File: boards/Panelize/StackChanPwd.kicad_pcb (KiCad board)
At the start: 2 copper layers, 50 x 87 mm, 45 parts, among them CN1 B2PS-VH, CN1 PinHeader, CN2 Grove, CN2 PinSocket, CN3 B3B-ZR, CN3 PinHeader, CN4 B3B-ZR, CN4 PinHeader, CN5 B3B-ZR, CN5 PinHeader, CN6 B3B-ZR, CN6 Grove, CN7 Grove, CN8 Grove, U1 74LVC2G125, U1 OKL-T/3-W12N, U2 74HCT2G125, U3 PCA9685PW

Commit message: fix panelized PCB
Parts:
- CN6: footprint Connector_JST:JST_PH_B4B-PH-K_1x04_P2.00mm_Vertical -> Grove:GROVE-HW4-2.0
- moved CN6 3.00 mm to (94.5, 88.0), turned to -90 degrees
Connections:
- CN6 pad 1: GND -> /SERIAL1
- CN6 pad 2: +5VM -> /SERIAL2
- CN6 pad 3: /SERIAL2 -> +5VM
- CN6 pad 4: /SERIAL1 -> GND
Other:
- rule pad_to_mask_clearance: 0 -> 0.051

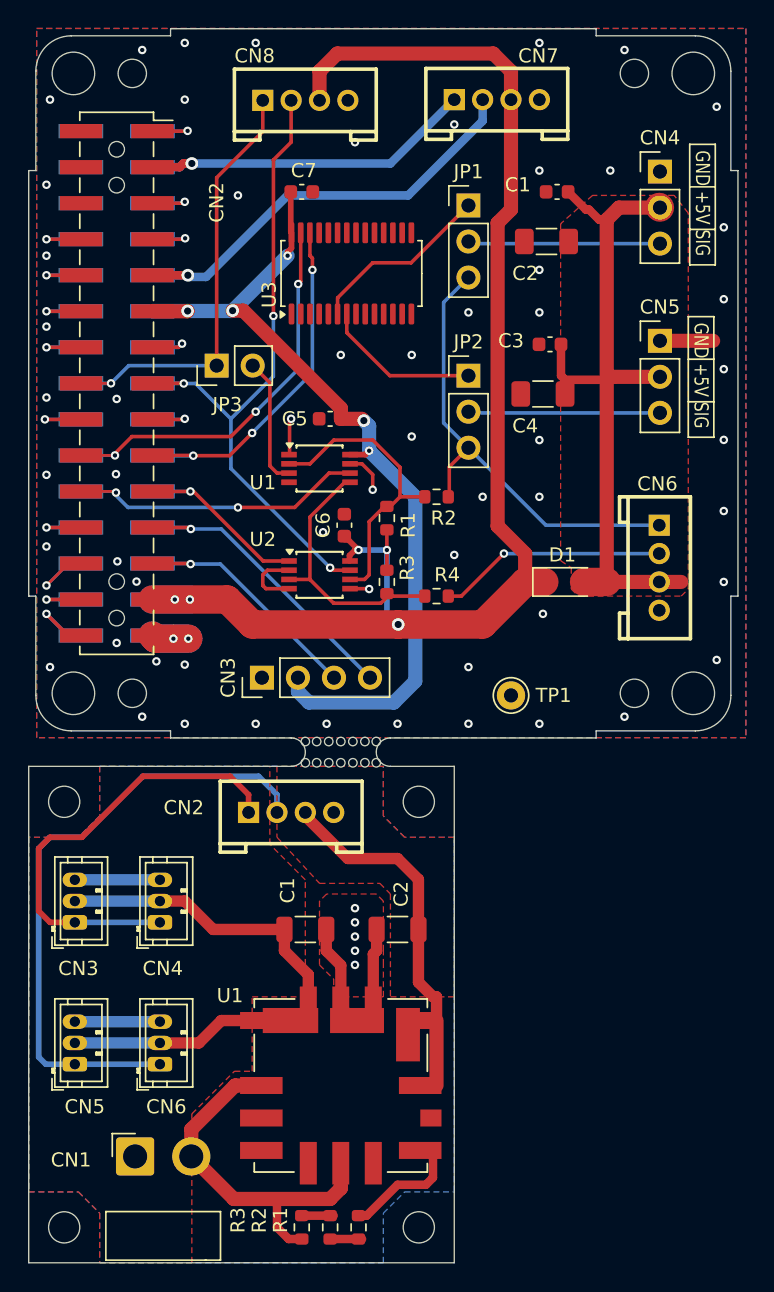
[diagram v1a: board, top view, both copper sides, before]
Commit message: fix PCB design (product ver1.0)
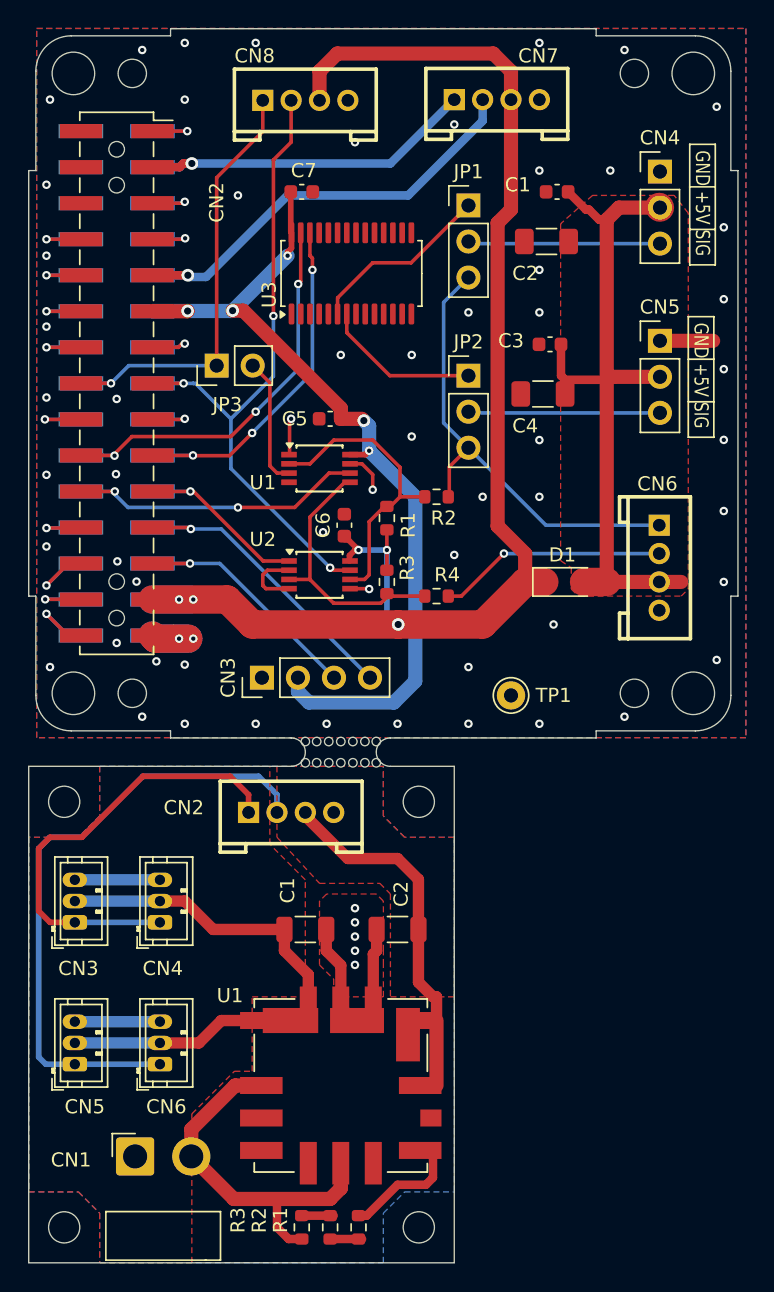
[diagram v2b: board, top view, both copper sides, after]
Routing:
- net /RXD2: track 32.9 -> 32.2 mm

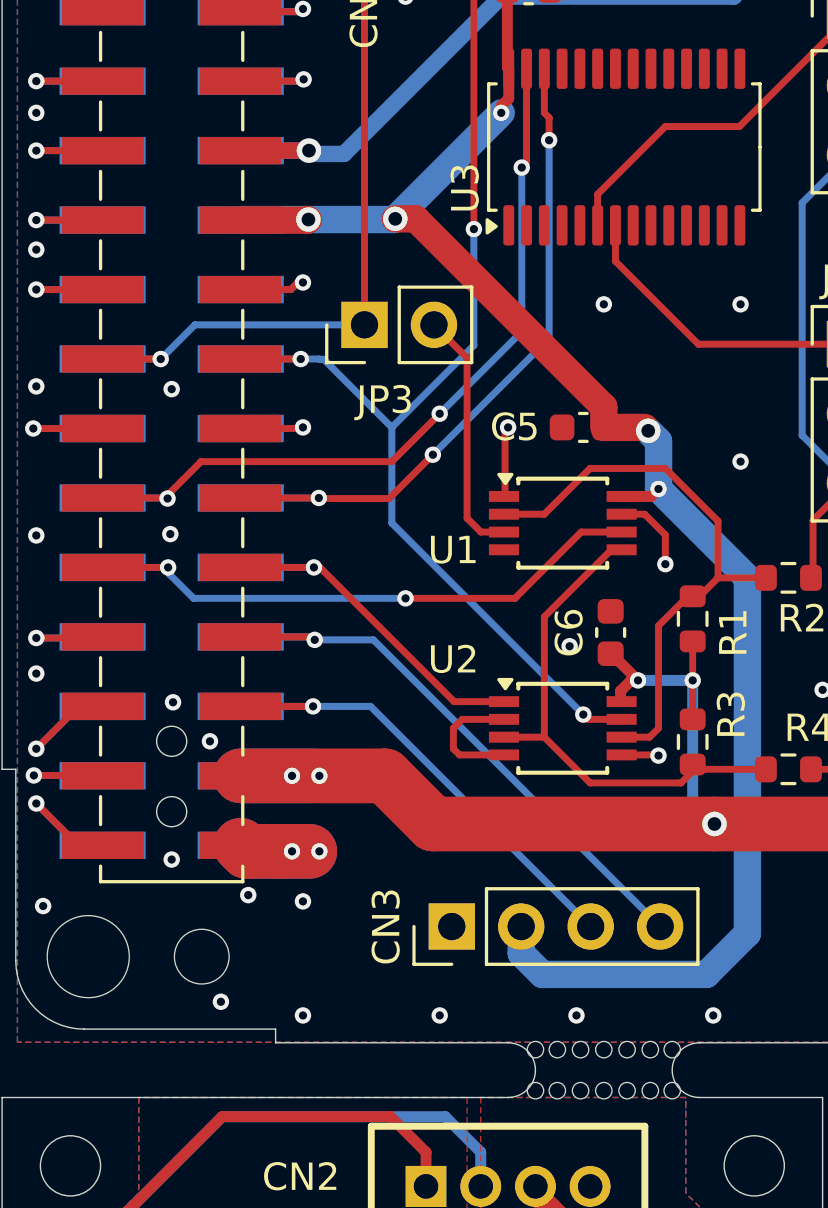
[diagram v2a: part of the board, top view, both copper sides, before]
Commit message: fix panelized PCB design
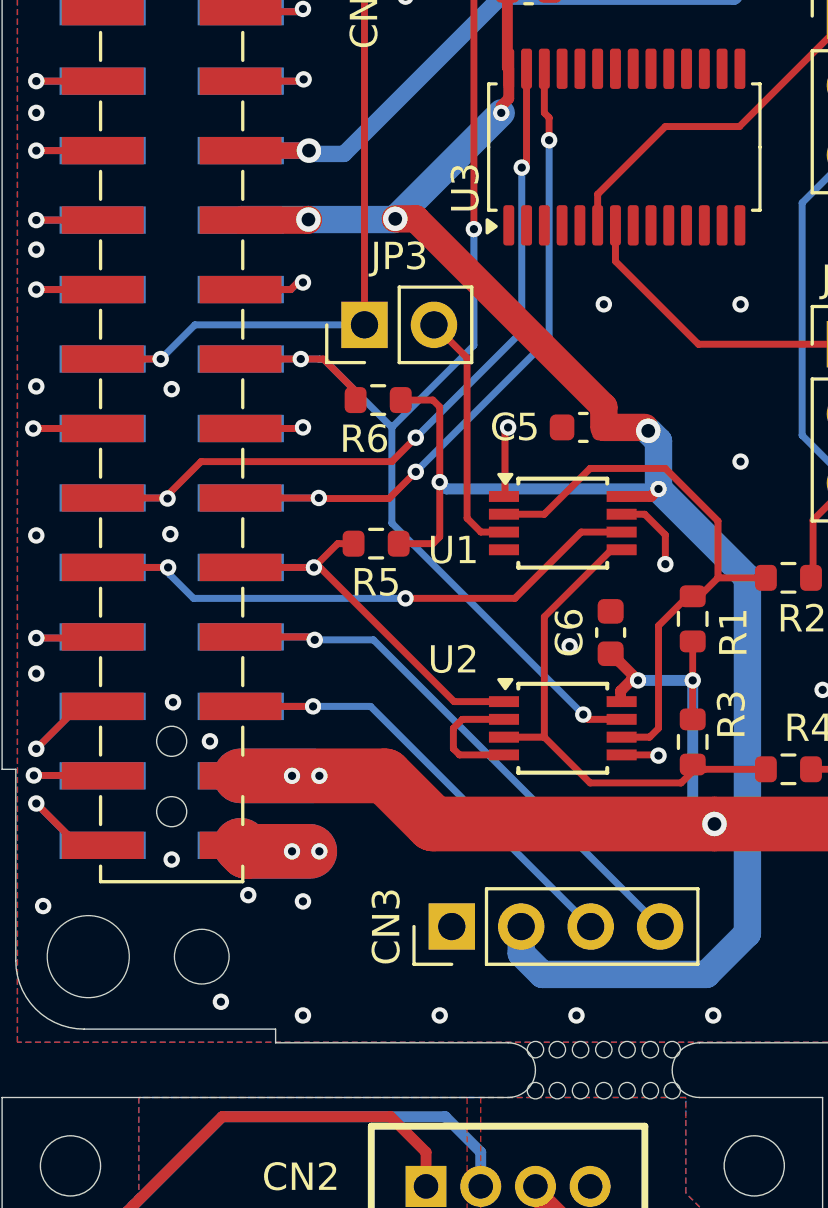
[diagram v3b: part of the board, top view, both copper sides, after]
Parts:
- added R5: 1k, Resistor_SMD:R_0603_1608Metric, F.Cu at (63.7, 81.8)
- added R6: 1k, Resistor_SMD:R_0603_1608Metric, F.Cu at (63.8, 76.5)
- CN4, CN5: value PinHeader -> B3B-EH-A
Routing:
- net +3V3: track 62.3 -> 78.3 mm, vias 5 -> 6
- net /TXD2: track 47.8 -> 50.6 mm
- net /TXD1: track 14.4 -> 16.2 mm
